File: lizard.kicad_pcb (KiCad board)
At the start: 2 copper layers, 22 x 98 mm, 23 parts, among them P1 SWD, U1 EFM8BB1

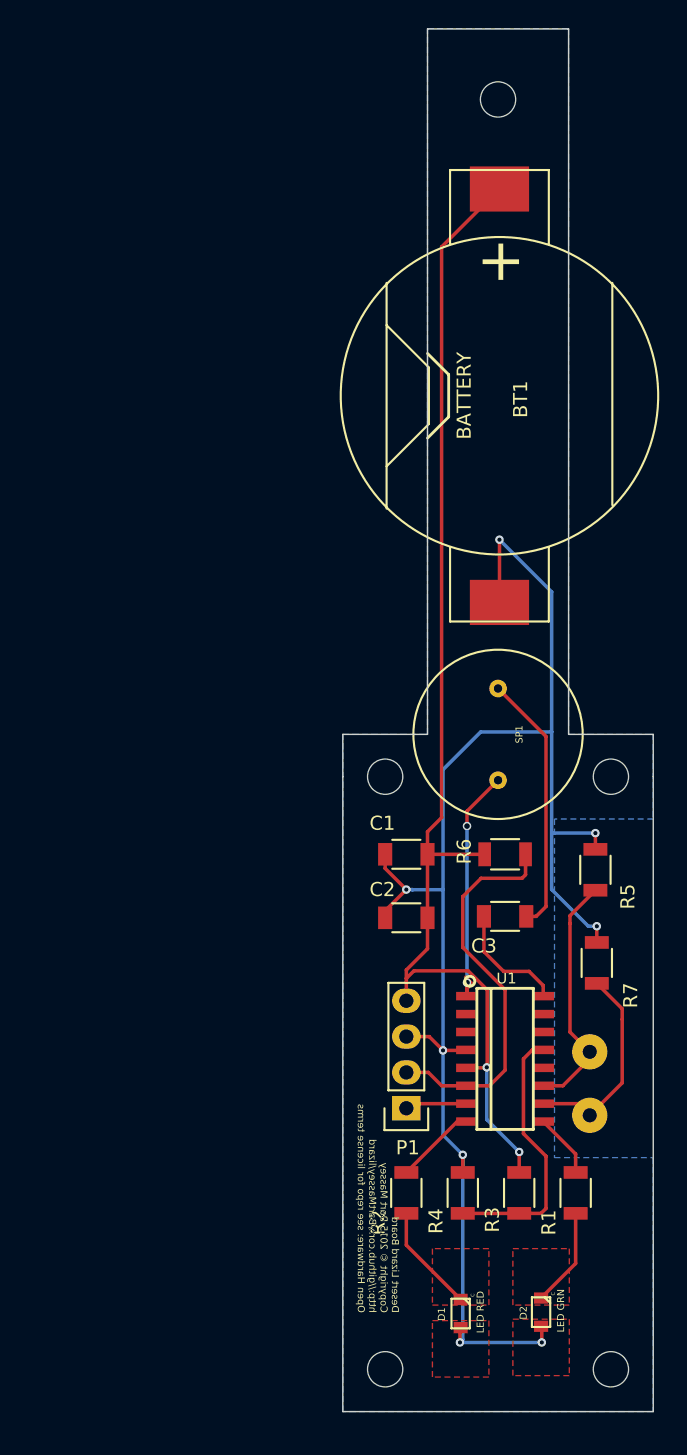
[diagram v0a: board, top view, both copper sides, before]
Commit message: updated to use extra board size; passed last check
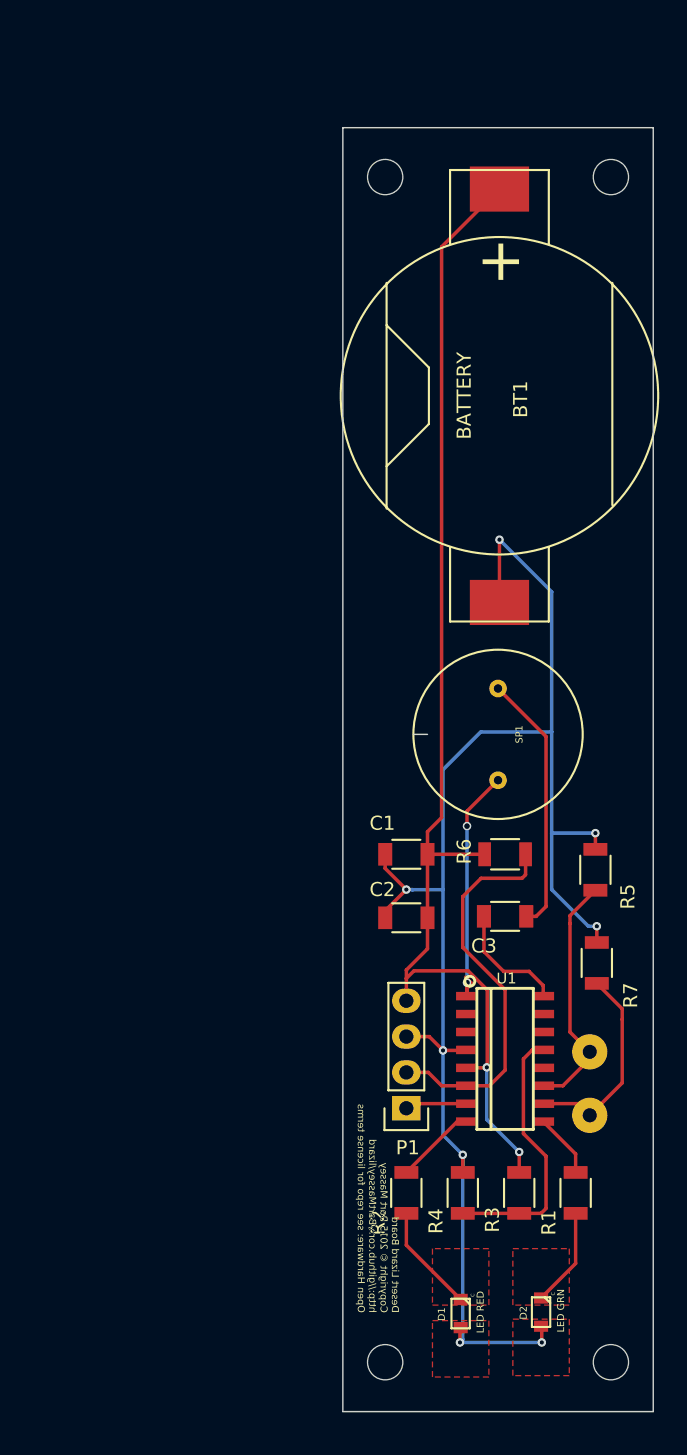
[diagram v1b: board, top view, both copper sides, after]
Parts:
- removed the REF** at (139.0, 113.0)
- moved REF** 42.5 mm to (155.0, 70.5)
- moved REF** 9.71 mm to (139.0, 70.5)
- moved REF** 0.50 mm to (155.0, 154.5)
- moved REF** 0.50 mm to (139.0, 154.5)
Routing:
- removed copper zone on B.Cu, net GND
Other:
- board size 22 x 98 mm -> 22 x 91 mm

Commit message: fixed bugs noticed during next OSHPark upload
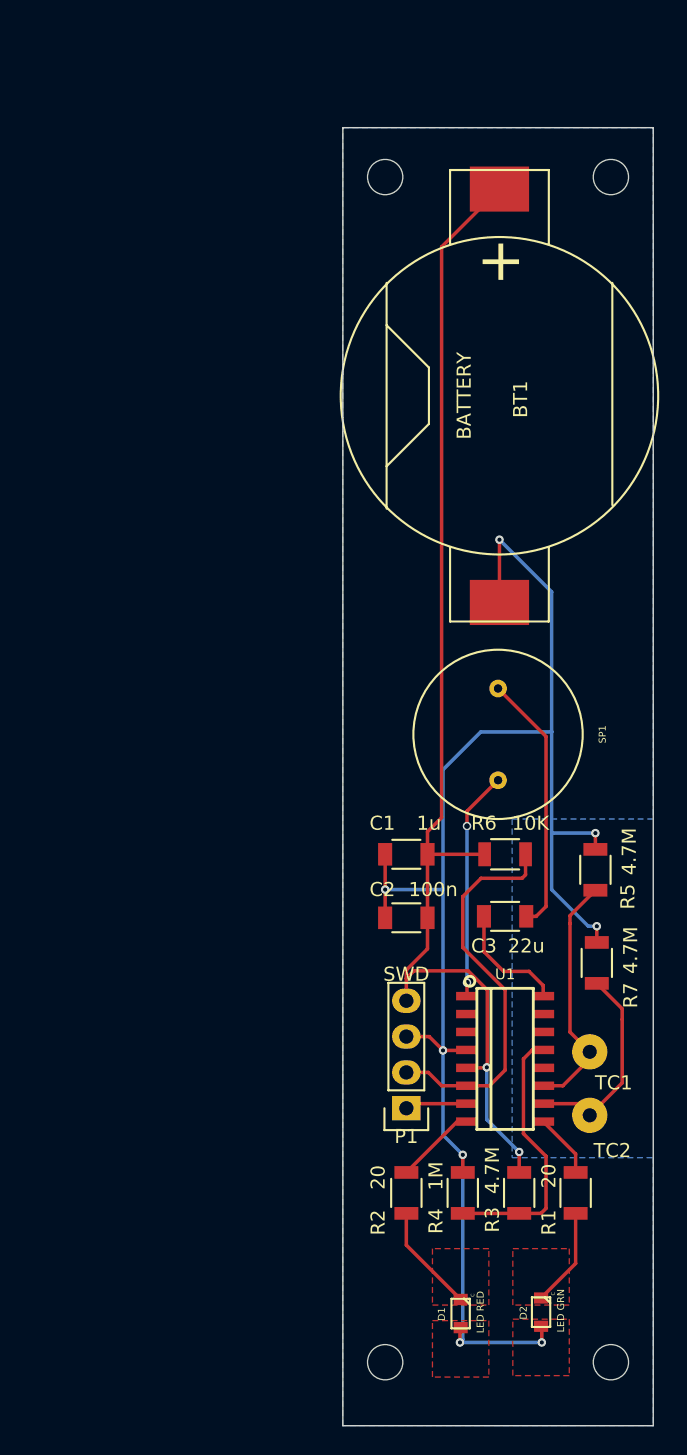
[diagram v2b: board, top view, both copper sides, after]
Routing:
- net Net-(SP1-Pad2): track 17.9 -> 16.2 mm
- net GND: track 113.2 -> 113.9 mm
- added copper zone on B.Cu, net GND
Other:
- board size 22 x 91 mm -> 22 x 92 mm
- board text added: "Desert Lizard Board v0.93 Copyright © 2015 Bart Massey http://github.com/BartMassey/lizard Open Hardware: see repo for license terms"
- board text removed: "Desert Lizard Board Copyright © 2015 Bart Massey http://github.com/BartMassey/lizard Open Hardware: see repo for license terms"

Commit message: increased speaker pin hole size; increased back text size
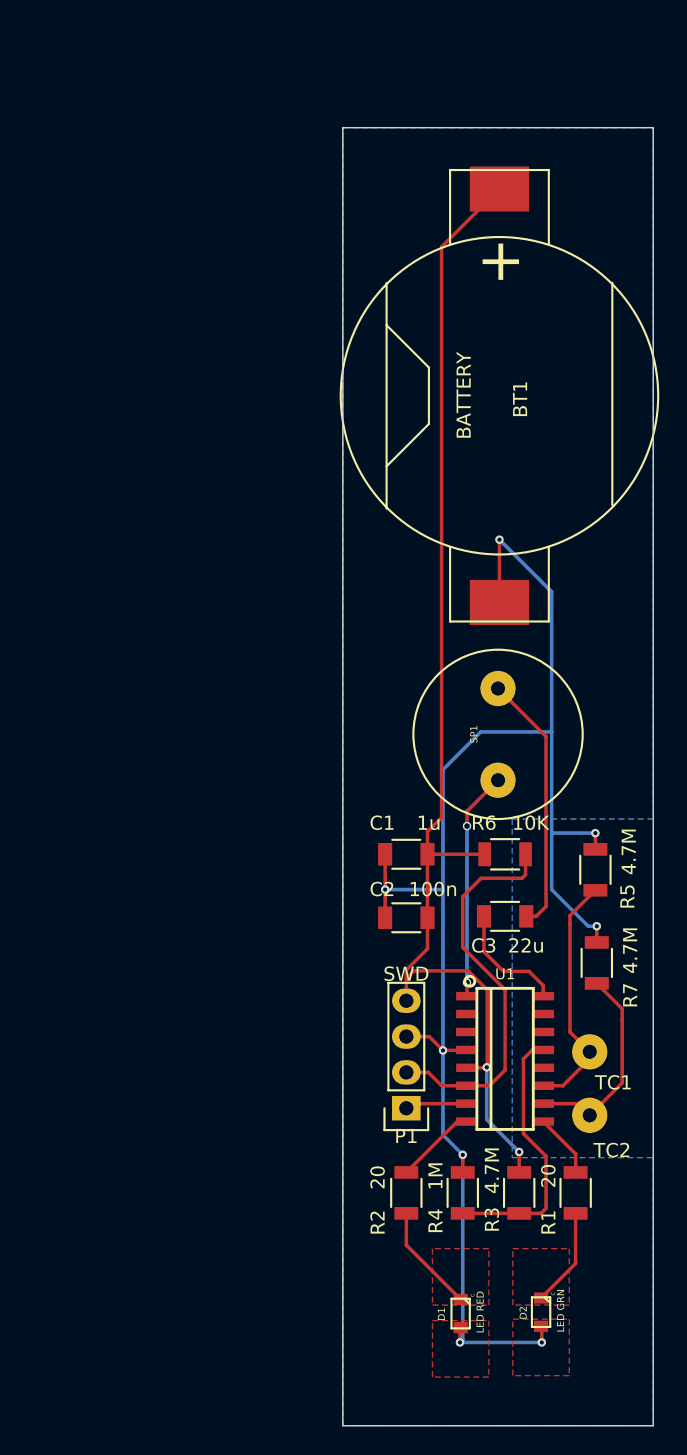
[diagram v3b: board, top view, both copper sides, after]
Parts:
- removed REF** (x4): MountingHole_2-5mm, Mounting_Holes:MountingHole_2-5mm
- turned SP1 to 90 degrees

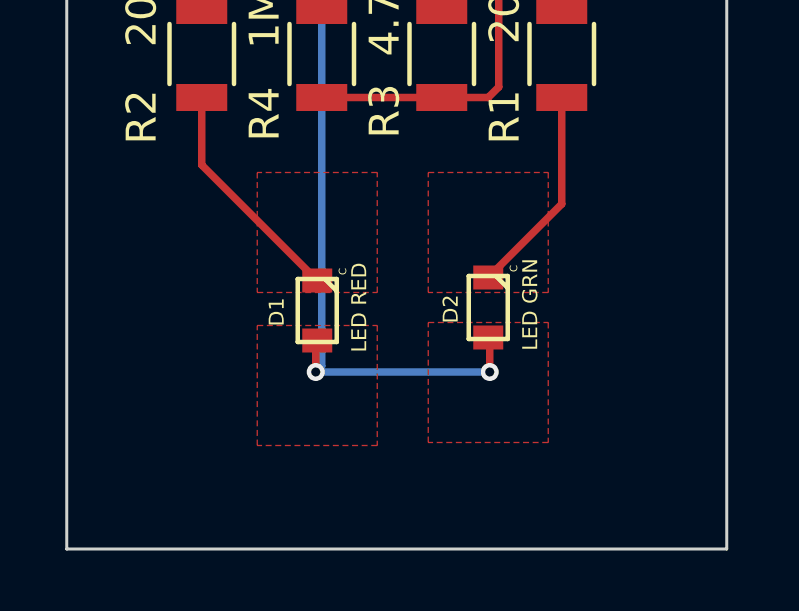
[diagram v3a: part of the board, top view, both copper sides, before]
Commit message: made improvements to front silk
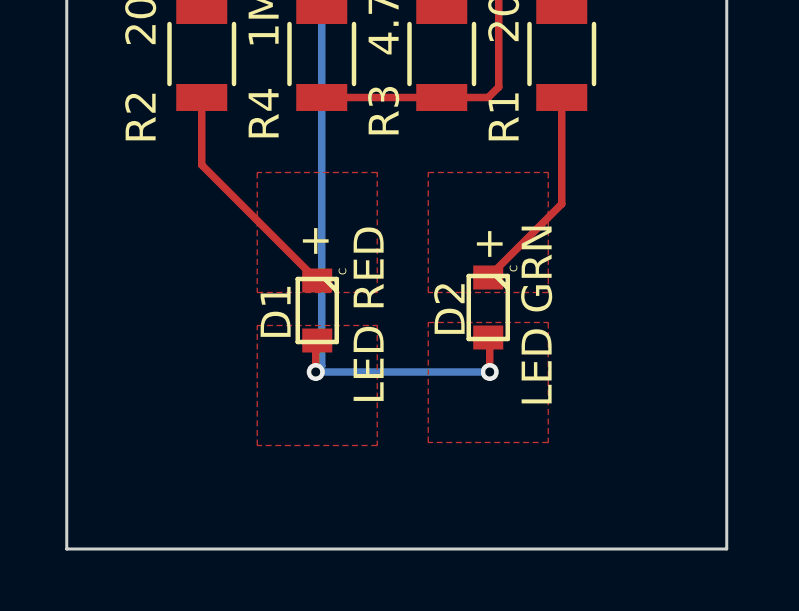
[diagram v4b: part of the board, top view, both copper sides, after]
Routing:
- net Net-(SP1-Pad2): track 16.2 -> 5.76 mm, vias 2 -> 0
- net Net-(C3-Pad2): track 18.5 -> 29.0 mm, vias 0 -> 2
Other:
- board text added: "+"

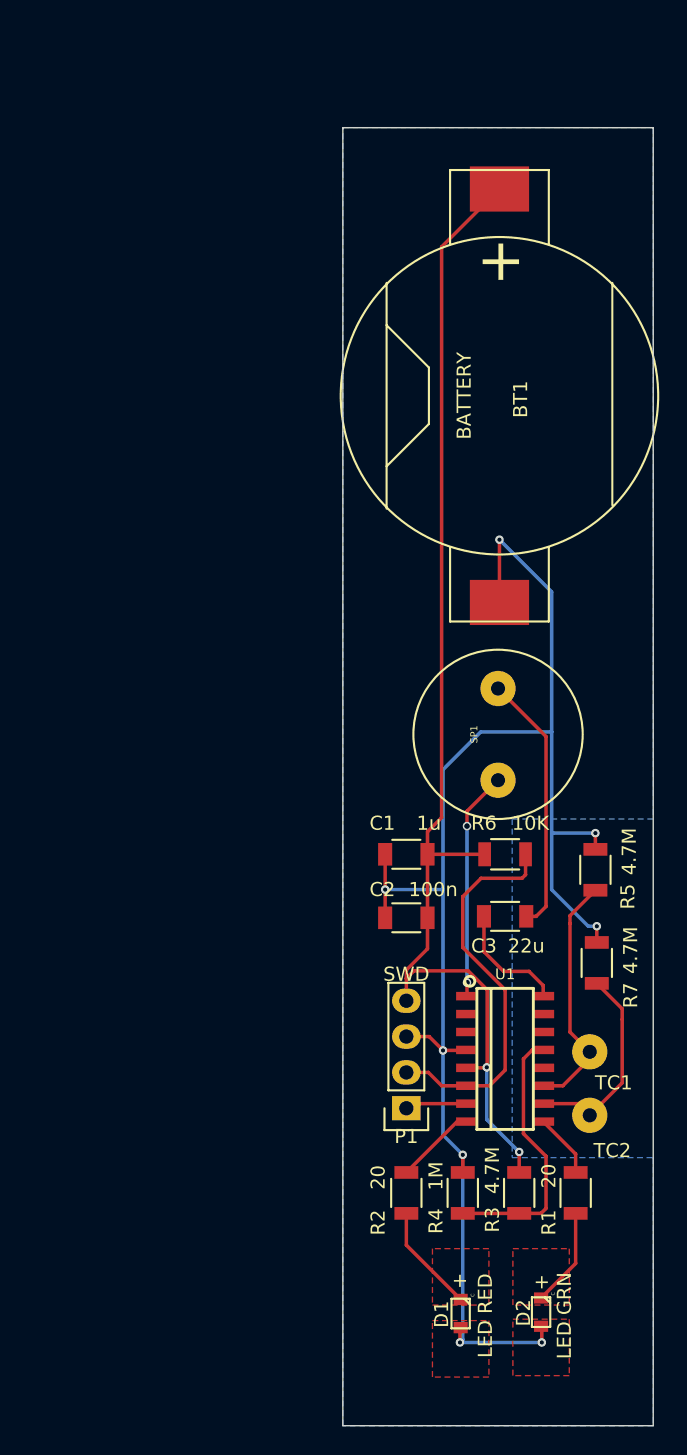
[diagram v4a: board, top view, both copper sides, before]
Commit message: finished cheesed redo of schematic and layout for v1.0 production board
This pass is the first at something that will eventually
look pretty much like the production PCB. Changes include
removing all the capacitors as gratuitous, removing the
gratuitous touchpad resistor, moving the battery to the back
and enlarging the tabs for hand soldering, moving to the new
LEDs, and changing to the USB Debug Device compatible debug
connector.

Changes for the next version include better re-layout with
less vias (maybe), removing the terrible debug connector as
too huge, and perhaps removing more components if
experimentation indicates.

The board id text is currently tiny and buried under the
battery once it's soldered on. Not much can be done, really.
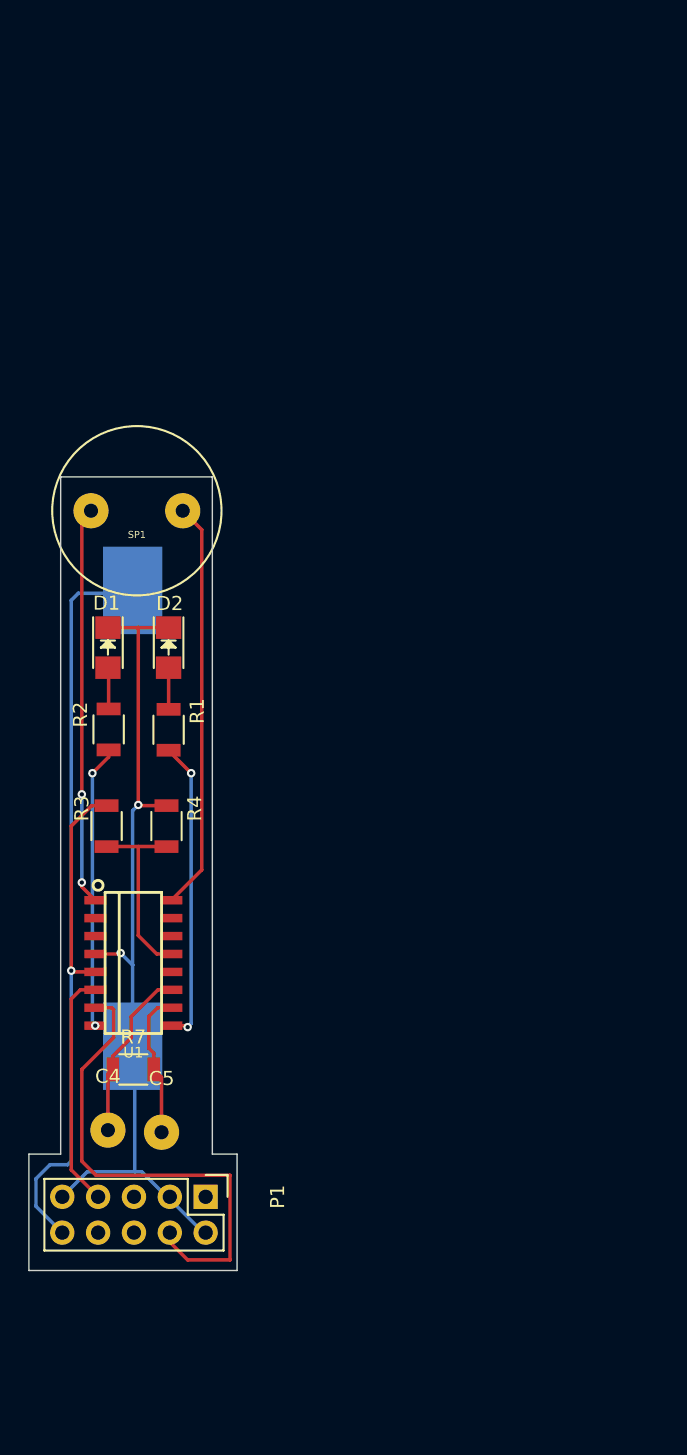
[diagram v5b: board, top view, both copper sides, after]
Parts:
- removed C1: 1u, Capacitors_SMD:C_1206
- removed C2: 100n, Capacitors_SMD:C_1206
- removed C3: 22u, Capacitors_SMD:C_1206
- removed R5: 4.7M, Resistors_SMD:R_1206
- removed R6: 10K, Resistors_SMD:R_1206
- BT1: moved to B.Cu
- D1, D2: footprint osram-m676:OSRAM-M676 -> LEDs:LED-1206
- P1: value SWD -> SW DBG; footprint Pin_Headers:Pin_Header_Straight_1x04 -> Pin_Headers:Pin_Header_Straight_2x05
- moved D2 54.0 mm to (123.7, 103.8), turned to 270 degrees
- moved D1 53.4 mm to (119.3, 103.8), turned to 270 degrees
- moved R1 43.7 mm to (123.7, 109.7), turned to 270 degrees
- moved BT1 39.7 mm to (121.1, 116.0)
- moved R3 39.1 mm to (119.2, 116.5)
- moved R2 39.0 mm to (119.4, 109.7), turned to 270 degrees
- moved C4 34.6 mm to (119.3, 138.1)
- moved R7 33.7 mm to (121.2, 133.8), turned to 0 degrees
- moved R4 33.4 mm to (123.5, 116.5)
- moved C5 30.4 mm to (123.2, 138.2)
- moved SP1 30.1 mm to (121.4, 94.2), turned to 180 degrees
- moved U1 27.2 mm to (121.2, 126.2)
- moved P1 15.5 mm to (126.3, 142.8), turned to 270 degrees
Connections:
- P1 pad 2: Net-(P1-Pad2) -> GND
- P1 pad 4: VDD -> Net-(P1-Pad4)
- R7 pad 1: Net-(C5-Pad1) -> Net-(C4-Pad1)
- R7 pad 2: GND -> Net-(C5-Pad1)
- SP1 pad 1: Net-(C3-Pad2) -> Net-(SP1-Pad1)
- U1 pad 16: Net-(C3-Pad1) -> Net-(SP1-Pad1)
- U1 pad 6: Net-(P1-Pad2) -> Net-(P1-Pad7)
- U1 pad 7: Net-(P1-Pad1) -> Net-(P1-Pad4)
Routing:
- net GND: track 113.9 -> 61.3 mm, vias 8 -> 2
- net Net-(P1-Pad4): track 0.00 -> 35.4 mm
- net Net-(SP1-Pad1): track 0.00 -> 29.1 mm
- net Net-(C3-Pad2): track 29.0 -> 0.00 mm, vias 2 -> 0
- net Net-(P1-Pad2): track 27.9 -> 0.00 mm
- net Net-(SP1-Pad2): track 5.76 -> 28.3 mm, vias 0 -> 2
- net VDD: track 86.3 -> 67.1 mm, vias 2 -> 1
- net Net-(R1-Pad2): track 4.56 -> 21.6 mm, vias 0 -> 2
- net Net-(P1-Pad7): track 0.00 -> 16.8 mm
- net Net-(R2-Pad2): track 5.79 -> 20.1 mm, vias 0 -> 2
- net Net-(C3-Pad1): track 8.45 -> 0.00 mm
- net Net-(R3-Pad2): track 19.0 -> 13.4 mm
- net Net-(C4-Pad1): track 17.4 -> 12.4 mm
- net Net-(D1-Pad2): track 7.69 -> 2.95 mm
- net Net-(P1-Pad1): track 4.43 -> 0.00 mm
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- removed copper zone on B.Cu, net GND
- removed copper zone on F.Cu, net GND
- removed copper zone on F.Cu, net Net-(D1-Pad2)
- removed copper zone on F.Cu, net Net-(D2-Pad2)
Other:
- board size 22 x 92 mm -> 14.8 x 56.2 mm
- board text added: "1.0"
- board text added: "2015-08-06"
- board text added: "Copyright © 2015 Bart Massey http://github.com/DesertLizard/LizardBoard Open Hardware: see repo for license terms"
- board text added: "Desert Lizard Board v1.0 Copyright © 2015 Bart Massey http://github.com/DesertLizard/LizardBoard"
- board text removed: "+"
- board text removed: "0.2"
- board text removed: "2014-06-11"
- board text removed: "Copyright © 2015 Bart Massey http://github.com/BartMassey/lizard Open Hardware: see repo for license terms"
- board text removed: "Desert Lizard Board v0.93 Copyright © 2015 Bart Massey http://github.com/BartMassey/lizard Open Hardware: see repo for license terms"
